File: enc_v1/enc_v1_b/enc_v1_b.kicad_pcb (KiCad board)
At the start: 2 copper layers, 24 x 15.5 mm, 6 parts, among them J2 Conn_01x09, U1 AS5047P-ATSM

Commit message: Connector changed
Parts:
- removed J2: Conn_01x09, Header:MOLEX_530480910
- added J1: 530481010, Header:CONN10_530481010_MOL, B.Cu at (143.3, 96.4)
- moved REF** 27.5 mm to (149.1, 108.0)
- moved REF** 27.5 mm to (143.2, 102.1)
- moved G*** 27.5 mm to (133.6, 98.6)
- moved U1 27.5 mm to (133.6, 100.5)
- moved C1 27.5 mm to (133.9, 105.1)
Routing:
- net /W/PWM: track 22.2 -> 21.2 mm
- net /A: track 19.3 -> 18.6 mm

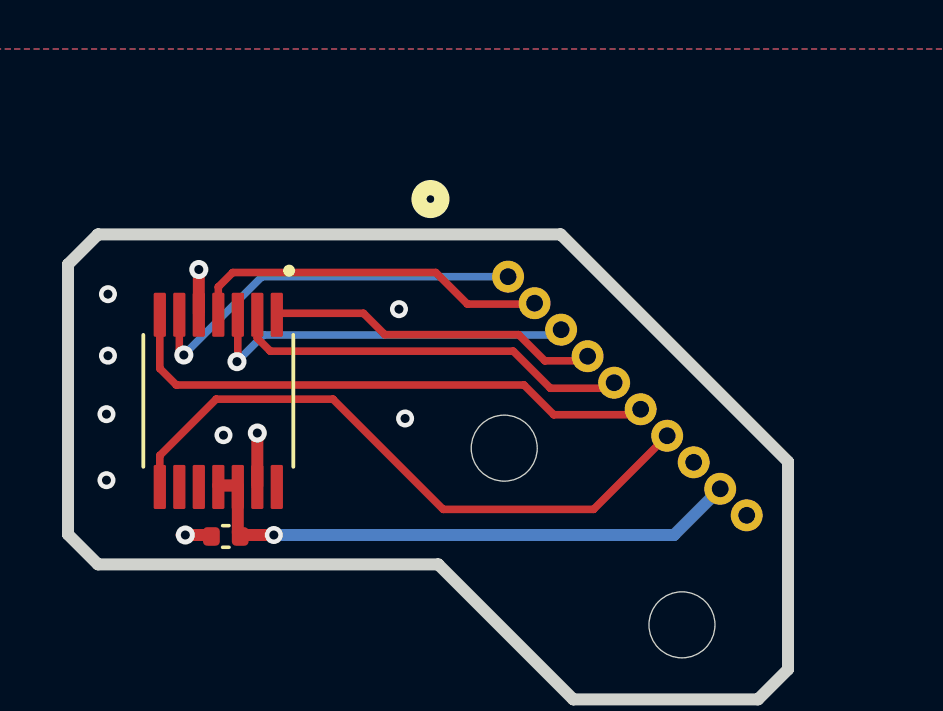
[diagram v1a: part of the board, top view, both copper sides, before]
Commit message: Connector footprint updated, fab files generated
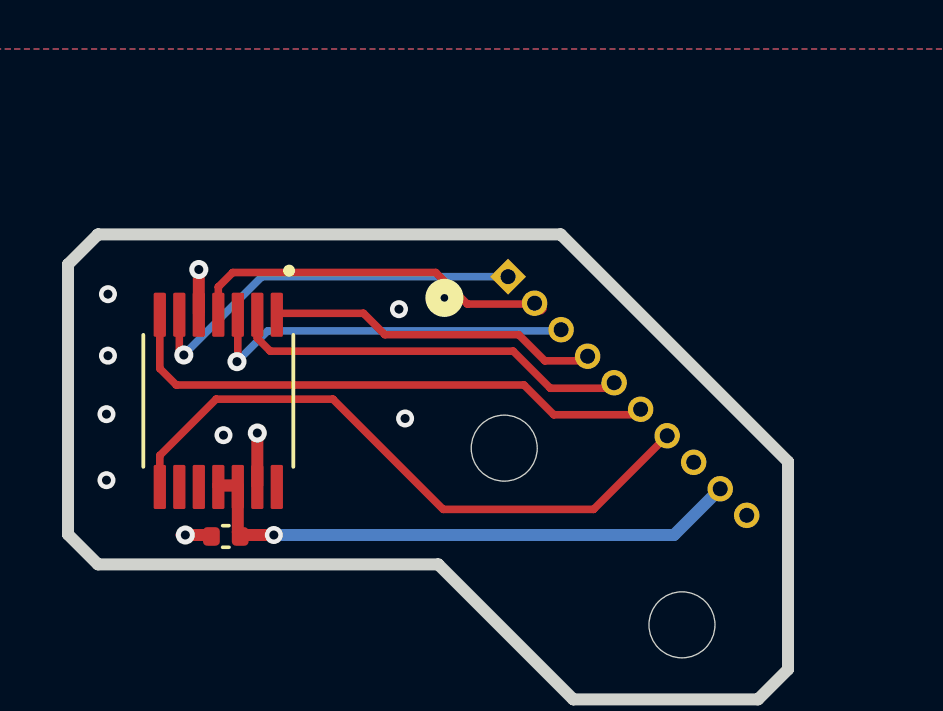
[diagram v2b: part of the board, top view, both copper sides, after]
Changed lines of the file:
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@@
 		(capping no)
 		(filling no)
-		(zone_defaults)
 		(pcbplotparams
 			(layerselection 0x00000000_00000000_55555555_5755f5ff)
@@
 			)
 		)
-		(property "Datasheet" "~"
+		(property "Datasheet" ""
 			(at 0 0 0)
 			(layer "F.Fab")
@@
 				(font
 					(size 1.27 1.27)
+					(thickness 0.15)
+				)
+			)
+		)
+		(property "JLCPCB" "C1525"
+			(at 0 0 180)
+			(unlocked yes)
+			(layer "F.Fab")
+			(hide yes)
+			(effects
+				(font
+					(size 1 1)
 					(thickness 0.15)
 				)
@@
 		(sheetname "/")
 		(sheetfile "enc_v1_b.kicad_sch")
+		(units
+			(unit
+				(name "A")
+				(pins "1" "2")
+			)
+		)
 		(attr smd)
 		(duplicate_pad_numbers_are_jumpers no)
@@
 			)
 		)
+		(property "JLCPCB" "C962063"
+			(at 0 0 270)
+			(unlocked yes)
+			(layer "F.Fab")
+			(hide yes)
+			(effects
+				(font
+					(size 1 1)
+					(thickness 0.15)
+				)
+			)
+		)
 		(sheetname "/")
 		(sheetfile "enc_v1_b.kicad_sch")
+		(units
+			(unit
+				(name "A")
+				(pins "2" "1" "4" "3" "5" "11" "12" "7" "6" "14" "10" "9" "8" "13")
+			)
+		)
 		(attr smd)
 		(duplicate_pad_numbers_are_jumpers no)
@@
 			(roundrect_rratio 0.125)
 			(net "/CSN")
-			(pinfunction "CSN")
+			(pinfunction "CSN_1")
 			(pintype "input")
 			(solder_mask_margin 0.102)
@@
 			(roundrect_rratio 0.125)
 			(net "/CLK")
-			(pinfunction "CLK")
+			(pinfunction "CLK_2")
 			(pintype "input")
 			(solder_mask_margin 0.102)
@@
 			(roundrect_rratio 0.125)
 			(net "/MISO")
-			(pinfunction "MISO")
+			(pinfunction "MISO_3")
 			(pintype "output")
 			(solder_mask_margin 0.102)
@@
 			(roundrect_rratio 0.125)
 			(net "/MOSI")
-			(pinfunction "MOSI")
+			(pinfunction "MOSI_4")
 			(pintype "input")
 			(solder_mask_margin 0.102)
@@
 			(roundrect_rratio 0.125)
 			(net "GND")
-			(pinfunction "TEST")
+			(pinfunction "TEST_5")
 			(pintype "passive")
 			(solder_mask_margin 0.102)
@@
 			(roundrect_rratio 0.125)
 			(net "/B")
-			(pinfunction "B")
+			(pinfunction "B_6")
 			(pintype "output")
 			(solder_mask_margin 0.102)
@@
 			(roundrect_rratio 0.125)
 			(net "/A")
-			(pinfunction "A")
+			(pinfunction "A_7")
 			(pintype "output")
 			(solder_mask_margin 0.102)
@@
 			(roundrect_rratio 0.125)
 			(net "/W{slash}PWM")
-			(pinfunction "W/PWM")
+			(pinfunction "W/PWM_8")
 			(pintype "output")
 			(solder_mask_margin 0.102)
@@
 			(roundrect_rratio 0.125)
 			(net "unconnected-(U1-V-Pad9)")
-			(pinfunction "V")
+			(pinfunction "V_9")
 			(pintype "output+no_connect")
 			(solder_mask_margin 0.102)
@@
 			(roundrect_rratio 0.125)
 			(net "unconnected-(U1-U-Pad10)")
-			(pinfunction "U")
+			(pinfunction "U_10")
 			(pintype "output+no_connect")
 			(solder_mask_margin 0.102)
@@
 			(roundrect_rratio 0.125)
 			(net "3v3")
-			(pinfunction "VDD")
+			(pinfunction "VDD_11")
 			(pintype "power_in")
 			(solder_mask_margin 0.102)
@@
 			(roundrect_rratio 0.125)
 			(net "3v3")
-			(pinfunction "VDD3V3")
+			(pinfunction "VDD3V3_12")
 			(pintype "power_in")
 			(solder_mask_margin 0.102)
@@
 			(roundrect_rratio 0.125)
 			(net "GND")
-			(pinfunction "GND")
+			(pinfunction "GND_13")
 			(pintype "power_in")
 			(solder_mask_margin 0.102)
@@
 			(roundrect_rratio 0.125)
 			(net "unconnected-(U1-I{slash}PWM-Pad14)")
-			(pinfunction "I/PWM")
+			(pinfunction "I/PWM_14")
 			(pintype "output+no_connect")
 			(solder_mask_margin 0.102)
@@
 		(tags "530481010 ")
 		(property "Reference" "J1"
-			(at 6.261149 1.937473 135)
+			(at 5.625001 0 135)
 			(unlocked yes)
 			(layer "B.SilkS")
@@
 				(font
 					(size 1.27 1.27)
+				)
+				(justify mirror)
+			)
+		)
+		(property "JLCPCB" ""
+			(at 0 0 315)
+			(unlocked yes)
+			(layer "B.Fab")
+			(hide yes)
+			(effects
+				(font
+					(size 1 1)
+					(thickness 0.15)
 				)
 				(justify mirror)
@@
 			)
 		)
-		(attr through_hole)
+		(attr through_hole exclude_from_pos_files exclude_from_bom)
 		(duplicate_pad_numbers_are_jumpers no)
 		(fp_circle
-			(center -3.658701 0)
-			(end -3.2777 0)
+			(center -1 2)
+			(end -0.618999 2)
 			(stroke
 				(width 0.508)
@@
 		)
 		(fp_circle
-			(center -3.658701 0)
-			(end -3.2777 0)
+			(center -1 2)
+			(end -0.8 2)
 			(stroke
 				(width 0.508)
@@
 		)
 		(fp_circle
-			(center 0 0)
-			(end 0.381 0)
+			(center 0 -1.5)
+			(end 0.381 -1.5)
 			(stroke
 				(width 0.508)
@@
 			)
 		)
-		(pad "1" thru_hole circle
+		(pad "1" thru_hole rect
 			(at 0 0 315)
-			(size 1.0668 1.0668)
-			(drill 0.5588)
+			(size 0.85 0.85)
+			(drill 0.5)
 			(layers "*.Cu" "*.Mask")
 			(remove_unused_layers no)
@@
 		(pad "2" thru_hole circle
 			(at 1.249999 0 315)
-			(size 1.0668 1.0668)
-			(drill 0.5588)
+			(size 0.85 0.85)
+			(drill 0.5)
 			(layers "*.Cu" "*.Mask")
 			(remove_unused_layers no)
@@
 		(pad "3" thru_hole circle
 			(at 2.5 0 315)
-			(size 1.0668 1.0668)
-			(drill 0.5588)
+			(size 0.85 0.85)
+			(drill 0.5)
 			(layers "*.Cu" "*.Mask")
 			(remove_unused_layers no)
@@
 		(pad "4" thru_hole circle
 			(at 3.749999 0 315)
-			(size 1.0668 1.0668)
-			(drill 0.5588)
+			(size 0.85 0.85)
+			(drill 0.5)
 			(layers "*.Cu" "*.Mask")
 			(remove_unused_layers no)
@@
 		(pad "5" thru_hole circle
 			(at 5 0 315)
-			(size 1.0668 1.0668)
-			(drill 0.5588)
+			(size 0.85 0.85)
+			(drill 0.5)
 			(layers "*.Cu" "*.Mask")
 			(remove_unused_layers no)
@@
 		(pad "6" thru_hole circle
 			(at 6.249999 0 315)
-			(size 1.0668 1.0668)
-			(drill 0.5588)
+			(size 0.85 0.85)
+			(drill 0.5)
 			(layers "*.Cu" "*.Mask")
 			(remove_unused_layers no)
@@
 		(pad "7" thru_hole circle
 			(at 7.5 0 315)
-			(size 1.0668 1.0668)
-			(drill 0.5588)
+			(size 0.85 0.85)
+			(drill 0.5)
 			(layers "*.Cu" "*.Mask")
 			(remove_unused_layers no)
@@
 		(pad "8" thru_hole circle
 			(at 8.75 0 315)
-			(size 1.0668 1.0668)
-			(drill 0.5588)
+			(size 0.85 0.85)
+			(drill 0.5)
 			(layers "*.Cu" "*.Mask")
 			(remove_unused_layers no)
@@
 		(pad "9" thru_hole circle
 			(at 10 0 315)
-			(size 1.0668 1.0668)
-			(drill 0.5588)
+			(size 0.85 0.85)
+			(drill 0.5)
 			(layers "*.Cu" "*.Mask")
 			(remove_unused_layers no)
@@
 		(pad "10" thru_hole circle
 			(at 11.25 0 315)
-			(size 1.0668 1.0668)
-			(drill 0.5588)
+			(size 0.85 0.85)
+			(drill 0.5)
 			(layers "*.Cu" "*.Mask")
 			(remove_unused_layers no)
@@
 		(model "${KIPRJMOD}/Libraries/53048-1010/KiCADv6/0530481010.stp"
 			(offset
-				(xyz 5.7 -5.5 0)
+				(xyz 5.62 -5.46 0.35)
 			)
 			(scale
@@
 	)
 	(segment
-		(start 135.135117 98.346883)
-		(end 144.874049 98.346883)
+		(start 135.272 98.21)
+		(end 145.010932 98.21)
 		(width 0.254)
 		(layer "B.Cu")
@@
 	)
 	(segment
-		(start 144.874049 98.346883)
+		(start 145.010932 98.21)
 		(end 145.050466 98.170466)
 		(width 0.254)
@@
 	)
 	(segment
-		(start 135.135117 98.346883)
-		(end 134.246 99.236)
-		(width 0.254)
-		(layer "B.Cu")
-		(net "/MISO")
-	)
-	(segment
-		(start 145.316 98.336)
-		(end 145.333767 98.353767)
-		(width 0.254)
-		(layer "B.Cu")
-		(net "/MISO")
-	)
-	(segment
-		(start 145.333767 98.353767)
-		(end 145.326883 98.346883)
+		(start 134.246 99.236)
+		(end 135.272 98.21)
 		(width 0.254)
 		(layer "B.Cu")
@@
 	)
 	(segment
-		(start 135.079301 96.402699)
+		(start 135.073301 96.402699)
 		(end 143.282699 96.402699)
 		(width 0.254)
@@
 	(segment
 		(start 132.474 99.008)
-		(end 135.079301 96.402699)
+		(end 132.474 99.002)
 		(width 0.254)
 		(layer "B.Cu")
+		(net "/B")
+	)
+	(segment
+		(start 132.474 99.002)
+		(end 135.073301 96.402699)
+		(width 0.254)
+		(layer "B.Cu")
